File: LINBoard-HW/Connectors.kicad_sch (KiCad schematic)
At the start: 5 parts, among them J2 USB_C_Receptacle_USB2.0, J4 ATM13-6P-BM03

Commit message: board layout started
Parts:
- D14: footprint (none) -> Diode_SMD:D_SOD-123
- J4: value ATM13-6P-BM03 -> ATM15-6P-BM03; footprint (none) -> ATM:ATM13-6P
- R13, R14: footprint Resistor_SMD:R_0603_1608Metric -> Resistor_SMD:R_0402_1005Metric
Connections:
- net ENABLE is gone; now on net CAN_H: J4.4 (Pin_4)
- net CAN_H: no longer J4.2 (Pin_2)
- net GND: now also J4.5 (Pin_5)
- net LIN: now also J4.2 (Pin_2); no longer J4.5 (Pin_5)
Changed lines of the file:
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@@
+	)
+	(junction
+		(at 57.15 50.8)
+		(diameter 0)
+		(color 0 0 0 0)
 	)
 	(junction
@@
 	(wire
 		(pts
-			(xy 58.42 50.8) (xy 58.42 54.61)
+			(xy 57.15 48.26) (xy 57.15 50.8)
 		)
 		(stroke
@@
 	(wire
 		(pts
-			(xy 60.96 38.1) (xy 58.42 38.1)
+			(xy 53.34 38.1) (xy 60.96 38.1)
 		)
 		(stroke
@@
 	(wire
 		(pts
-			(xy 60.96 50.8) (xy 58.42 50.8)
-		)
-		(stroke
-			(width 0)
-			(type default)
-		)
-	)
-	(wire
-		(pts
 			(xy 54.61 113.03) (xy 63.5 113.03)
 		)
@@
 	(wire
 		(pts
+			(xy 57.15 50.8) (xy 60.96 50.8)
+		)
+		(stroke
+			(width 0)
+			(type default)
+		)
+	)
+	(wire
+		(pts
 			(xy 54.61 128.27) (xy 63.5 128.27)
 		)
@@
 	(wire
 		(pts
-			(xy 58.42 38.1) (xy 58.42 35.56)
+			(xy 57.15 50.8) (xy 57.15 58.42)
+		)
+		(stroke
+			(width 0)
+			(type default)
+		)
+	)
+	(wire
+		(pts
+			(xy 60.96 48.26) (xy 57.15 48.26)
+		)
+		(stroke
+			(width 0)
+			(type default)
+		)
+	)
+	(wire
+		(pts
+			(xy 53.34 38.1) (xy 53.34 35.56)
 		)
 		(stroke
@@
 	(hierarchical_label "CAN_H"
 		(shape bidirectional)
-		(at 60.96 40.64 180)
-		(effects
-			(font
-				(size 1.27 1.27)
-			)
-			(justify right)
-		)
-	)
-	(hierarchical_label "ENABLE"
-		(shape output)
 		(at 60.96 45.72 180)
 		(effects
@@
 	(hierarchical_label "LIN"
 		(shape bidirectional)
-		(at 60.96 48.26 180)
+		(at 60.96 40.64 180)
 		(effects
 			(font
@@
 			)
 		)
-		(property "Footprint" ""
+		(property "Footprint" "Diode_SMD:D_SOD-123"
 			(at 66.04 113.03 90)
 			(effects
@@
 	(symbol
 		(lib_id "power:+12V")
-		(at 58.42 35.56 0)
+		(at 53.34 35.56 0)
 		(unit 1)
 		(exclude_from_sim no)
@@
 		(on_board yes)
 		(dnp no)
-		(fields_autoplaced yes)
 		(property "Reference" "#PWR018"
-			(at 58.42 39.37 0)
+			(at 53.34 39.37 0)
 			(effects
 				(font
@@
 		)
 		(property "Value" "+12V"
-			(at 58.42 30.48 0)
+			(at 53.086 31.75 0)
 			(effects
 				(font
@@
 		)
 		(property "Footprint" ""
-			(at 58.42 35.56 0)
+			(at 53.34 35.56 0)
 			(effects
 				(font
@@
 		)
 		(property "Datasheet" ""
-			(at 58.42 35.56 0)
+			(at 53.34 35.56 0)
 			(effects
 				(font
@@
 		)
 		(property "Description" "Power symbol creates a global label with name \"+12V\""
-			(at 58.42 35.56 0)
+			(at 53.34 35.56 0)
 			(effects
 				(font
@@
 	(symbol
 		(lib_id "power:GND")
-		(at 58.42 54.61 0)
+		(at 57.15 58.42 0)
 		(unit 1)
 		(exclude_from_sim no)
@@
 		(fields_autoplaced yes)
 		(property "Reference" "#PWR019"
-			(at 58.42 60.96 0)
+			(at 57.15 64.77 0)
 			(effects
 				(font
@@
 		)
 		(property "Value" "GND"
-			(at 58.42 59.69 0)
+			(at 57.15 63.5 0)
 			(effects
 				(font
@@
 		)
 		(property "Footprint" ""
-			(at 58.42 54.61 0)
+			(at 57.15 58.42 0)
 			(effects
 				(font
@@
 		)
 		(property "Datasheet" ""
-			(at 58.42 54.61 0)
+			(at 57.15 58.42 0)
 			(effects
 				(font
@@
 		)
 		(property "Description" "Power symbol creates a global label with name \"GND\" , ground"
-			(at 58.42 54.61 0)
+			(at 57.15 58.42 0)
 			(effects
 				(font
@@
 			)
 		)
-		(property "Value" "ATM13-6P-BM03"
+		(property "Value" "ATM15-6P-BM03"
 			(at 68.58 45.7199 0)
 			(effects
@@
 			)
 		)
-		(property "Footprint" ""
+		(property "Footprint" "ATM:ATM13-6P"
 			(at 66.04 43.18 0)
 			(effects
@@
 			)
 		)
-		(property "Footprint" "Resistor_SMD:R_0603_1608Metric"
+		(property "Footprint" "Resistor_SMD:R_0402_1005Metric"
 			(at 80.01 123.19 0)
 			(effects
@@
 			)
 		)
-		(property "Footprint" "Resistor_SMD:R_0603_1608Metric"
+		(property "Footprint" "Resistor_SMD:R_0402_1005Metric"
 			(at 90.17 123.19 0)
 			(effects

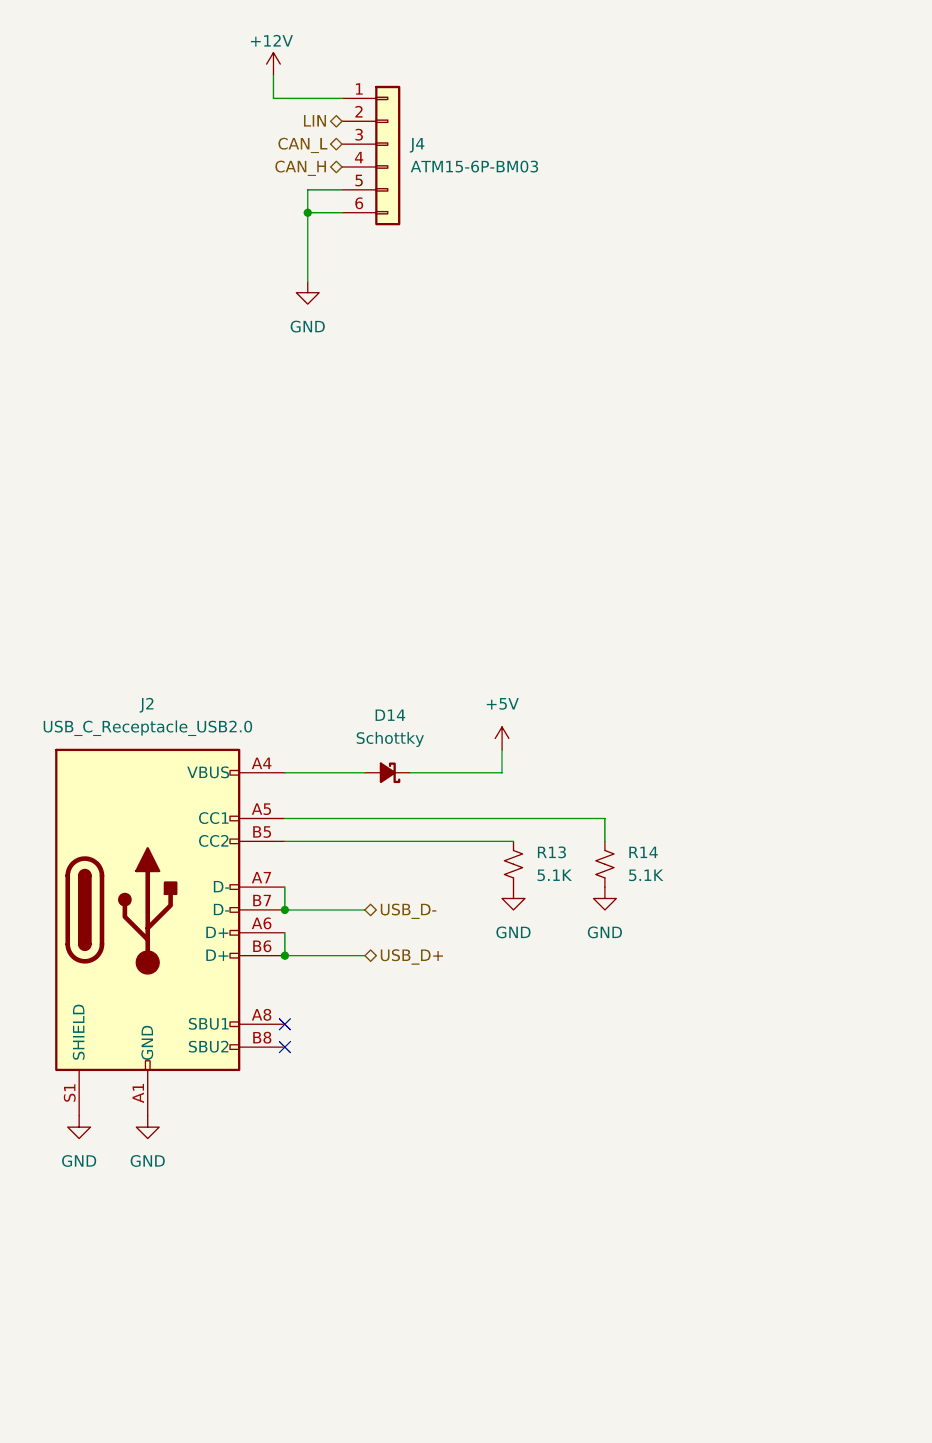
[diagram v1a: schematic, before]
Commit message: change usb
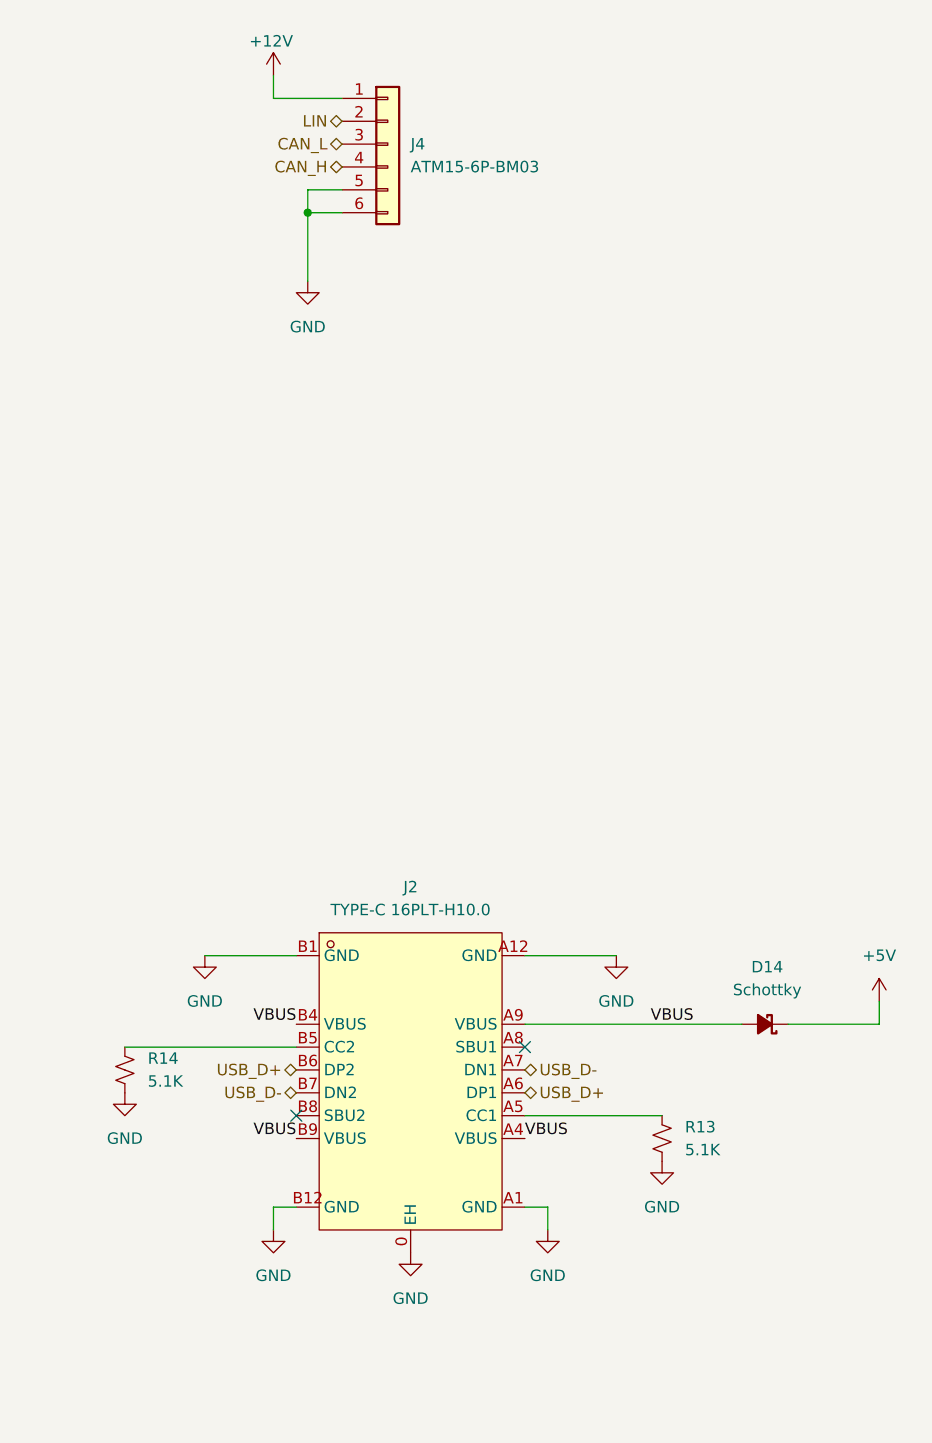
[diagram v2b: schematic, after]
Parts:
- removed J2: USB_C_Receptacle_USB2.0, Connector_USB:USB_C_Receptacle_GCT_USB4085, symbol Connectors:USB_C_Receptacle_USB2.0
- added J2: TYPE-C 16PLT-H10.0, vert_usb:TYPE-C-SMD_USB4120-03-C, symbol vert_usb:TYPE-C16PLT-H10.0
- J4: footprint ATM:ATM13-6P -> ATM:ATM15-6P_NoMountingHoles
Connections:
- net GND: now also J2.0 (EH), J2.A1 (GND), J2.A12 (GND), J2.B1 (GND), J2.B12 (GND)
- net USB_D+: now also J2.A6 (DP1), J2.B6 (DP2)
- net USB_D-: now also J2.A7 (DN1), J2.B7 (DN2)
- net VBUS: now reaches D14.2 (A)
- net VBUS: now also J2.A4 (VBUS), J2.A9 (VBUS), J2.B4 (VBUS), J2.B9 (VBUS)
- net at R14.1: now also J2.B5 (CC2)
- net at R13.1: now also J2.A5 (CC1)
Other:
- moved on the sheet: D14, R13, R14

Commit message: back to ra connectors
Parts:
- J2: footprint vert_usb:TYPE-C-SMD_USB4120-03-C -> Connector_USB:USB_C_Receptacle_GCT_USB4085
- J4: footprint ATM:ATM15-6P_NoMountingHoles -> ATM:ATM13-6P
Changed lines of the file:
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@@
 			)
 		)
-		(property "Footprint" "vert_usb:TYPE-C-SMD_USB4120-03-C"
+		(property "Footprint" "Connector_USB:USB_C_Receptacle_GCT_USB4085"
 			(at 68.58 173.99 0)
 			(effects
@@
 			)
 		)
-		(property "Footprint" "ATM:ATM15-6P_NoMountingHoles"
+		(property "Footprint" "ATM:ATM13-6P"
 			(at 66.04 43.18 0)
 			(effects

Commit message: doing some layout
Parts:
- R13, R14: footprint Resistor_SMD:R_0402_1005Metric -> Resistor_SMD:R_0805_2012Metric
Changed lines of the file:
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@@
 			)
 		)
-		(property "Footprint" "Resistor_SMD:R_0402_1005Metric"
+		(property "Footprint" "Resistor_SMD:R_0805_2012Metric"
 			(at 96.52 153.67 0)
 			(effects
@@
 			)
 		)
-		(property "Footprint" "Resistor_SMD:R_0402_1005Metric"
+		(property "Footprint" "Resistor_SMD:R_0805_2012Metric"
 			(at 36.83 146.05 0)
 			(effects

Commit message: routing first pass complete
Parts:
- removed J2: TYPE-C 16PLT-H10.0, Connector_USB:USB_C_Receptacle_GCT_USB4085, symbol vert_usb:TYPE-C16PLT-H10.0
- added J3: USB_C_Receptacle_USB2.0, Connector_USB:USB_C_Receptacle_GCT_USB4085, symbol Connectors:USB_C_Receptacle_USB2.0
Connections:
- net +12V: now also J4.6 (Pin_6); no longer J4.1 (Pin_1)
- net CAN_H: now also J4.2 (Pin_2); no longer J4.4 (Pin_4)
- net CAN_L: now also J4.1 (Pin_1); no longer J4.3 (Pin_3)
- net GND: now also J4.4 (Pin_4), J3.A1 (GND), J3.A12 (GND), J3.B1 (GND), J3.B12 (GND), J3.S1 (SHIELD); no longer J4.6 (Pin_6)
- net LIN: now also J4.3 (Pin_3); no longer J4.2 (Pin_2)
- net USB_D+: now also J3.A6 (D+), J3.B6 (D+)
- net USB_D-: now also J3.A7 (D-), J3.B7 (D-)
- net VBUS: now also J3.A4 (VBUS), J3.A9 (VBUS), J3.B4 (VBUS), J3.B9 (VBUS)
- net at R13.1: now also J3.A5 (CC1)
- net at R14.1: now also J3.B5 (CC2)
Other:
- moved on the sheet: D14, R13, R14

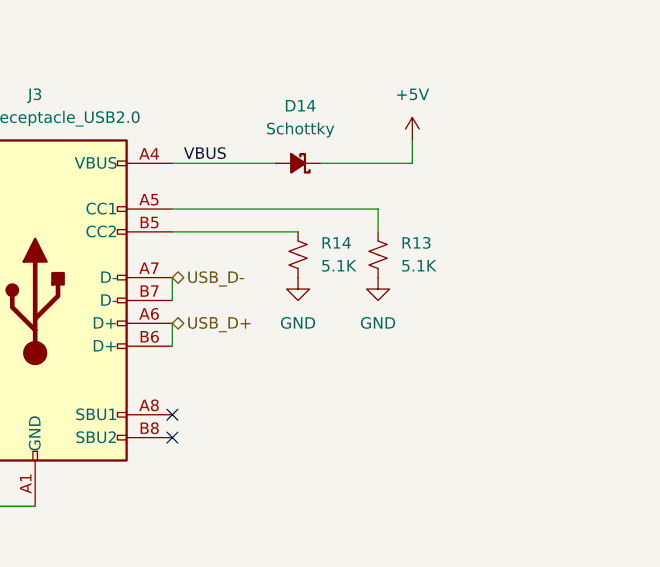
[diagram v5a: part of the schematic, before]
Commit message: fixed some trace widths
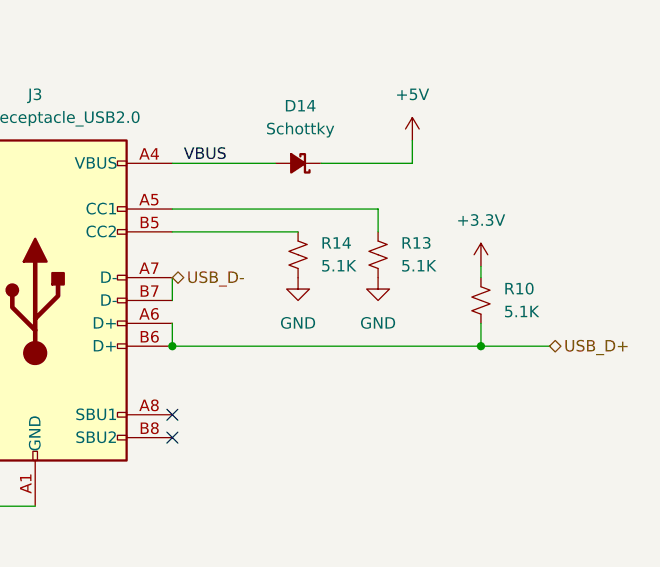
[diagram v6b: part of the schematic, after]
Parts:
- added R10: 5.1K, Resistor_SMD:R_0805_2012Metric, symbol Device:R_Small_US
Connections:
- net USB_D+: now also R10.2
- new net +3.3V: R10.1
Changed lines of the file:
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@@
+	)
+	(junction
+		(at 106.68 161.29)
+		(diameter 0)
+		(color 0 0 0 0)
 	)
 	(junction
@@
 		(color 0 0 0 0)
 	)
+	(junction
+		(at 72.39 161.29)
+		(diameter 0)
+		(color 0 0 0 0)
+	)
 	(no_connect
 		(at 72.39 168.91)
@@
 	(wire
 		(pts
+			(xy 106.68 158.75) (xy 106.68 161.29)
+		)
+		(stroke
+			(width 0)
+			(type default)
+		)
+	)
+	(wire
+		(pts
+			(xy 106.68 161.29) (xy 114.3 161.29)
+		)
+		(stroke
+			(width 0)
+			(type default)
+		)
+	)
+	(wire
+		(pts
+			(xy 106.68 152.4) (xy 106.68 153.67)
+		)
+		(stroke
+			(width 0)
+			(type default)
+		)
+	)
+	(wire
+		(pts
 			(xy 72.39 146.05) (xy 95.25 146.05)
 		)
@@
 		(pts
 			(xy 60.96 58.42) (xy 66.04 58.42)
+		)
+		(stroke
+			(width 0)
+			(type default)
+		)
+	)
+	(wire
+		(pts
+			(xy 72.39 161.29) (xy 106.68 161.29)
 		)
 		(stroke
@@
 	(hierarchical_label "USB_D+"
 		(shape bidirectional)
-		(at 72.39 158.75 0)
+		(at 114.3 161.29 0)
 		(effects
 			(font
@@
 	)
 	(symbol
+		(lib_id "power:+3.3V")
+		(at 106.68 152.4 0)
+		(unit 1)
+		(exclude_from_sim no)
+		(in_bom yes)
+		(on_board yes)
+		(dnp no)
+		(fields_autoplaced yes)
+		(property "Reference" "#PWR031"
+			(at 106.68 156.21 0)
+			(effects
+				(font
+					(size 1.27 1.27)
+				)
+				(hide yes)
+			)
+		)
+		(property "Value" "+3.3V"
+			(at 106.68 147.32 0)
+			(effects
+				(font
+					(size 1.27 1.27)
+				)
+			)
+		)
+		(property "Footprint" ""
+			(at 106.68 152.4 0)
+			(effects
+				(font
+					(size 1.27 1.27)
+				)
+				(hide yes)
+			)
+		)
+		(property "Datasheet" ""
+			(at 106.68 152.4 0)
+			(effects
+				(font
+					(size 1.27 1.27)
+				)
+				(hide yes)
+			)
+		)
+		(property "Description" "Power symbol creates a global label with name \"+3.3V\""
+			(at 106.68 152.4 0)
+			(effects
+				(font
+					(size 1.27 1.27)
+				)
+				(hide yes)
+			)
+		)
+		(pin "1"
+		)
+		(instances
+			(project "LINBoard-HW"
+				(path "/27863e5d-8a22-474c-850d-36d8970b0f4a/33375ab4-d724-4202-b76f-e99edd78e94c"
+					(reference "#PWR031")
+					(unit 1)
+				)
+			)
+		)
+	)
+	(symbol
 		(lib_id "power:GND")
 		(at 49.53 179.07 0)
@@
 					(unit 1)
 				)
+			)
+		)
+	)
+	(symbol
+		(lib_id "Device:R_Small_US")
+		(at 106.68 156.21 0)
+		(unit 1)
+		(exclude_from_sim no)
+		(in_bom yes)
+		(on_board yes)
+		(dnp no)
+		(fields_autoplaced yes)
+		(property "Reference" "R10"
+			(at 109.22 154.9399 0)
+			(effects
+				(font
+					(size 1.27 1.27)
+				)
+				(justify left)
+			)
+		)
+		(property "Value" "5.1K"
+			(at 109.22 157.4799 0)
+			(effects
+				(font
+					(size 1.27 1.27)
+				)
+				(justify left)
+			)
+		)
+		(property "Footprint" "Resistor_SMD:R_0805_2012Metric"
+			(at 106.68 156.21 0)
+			(effects
+				(font
+					(size 1.27 1.27)
+				)
+				(hide yes)
+			)
+		)
+		(property "Datasheet" "~"
+			(at 106.68 156.21 0)
+			(effects
+				(font
+					(size 1.27 1.27)
+				)
+				(hide yes)
+			)
+		)
+		(property "Description" "Resistor, small US symbol"
+			(at 106.68 156.21 0)
+			(effects
+				(font
+					(size 1.27 1.27)
+				)
+				(hide yes)
+			)
+		)
+		(pin "2"
+		)
+		(pin "1"
+		)
+		(instances
+			(project "LINBoard-HW"
+				(path "/27863e5d-8a22-474c-850d-36d8970b0f4a/33375ab4-d724-4202-b76f-e99edd78e94c"
+					(reference "R10")
+					(unit 1)
+				)

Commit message: add fab outputs
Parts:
- D14: LCSC Part (none) -> C179426
- J3, J4: now left out of the parts list
- R10, R13, R14: LCSC Part (none) -> C218638
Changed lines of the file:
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@@
+			)
+		)
+		(property "LCSC Part" "C179426"
+			(at 86.36 140.97 0)
+			(effects
+				(font
+					(size 1.27 1.27)
+				)
+				(hide yes)
 			)
 		)
@@
 		(unit 1)
 		(exclude_from_sim no)
-		(in_bom yes)
+		(in_bom no)
 		(on_board yes)
 		(dnp no)
@@
 			)
 		)
+		(property "LCSC Part" ""
+			(at 66.04 43.18 0)
+			(effects
+				(font
+					(size 1.27 1.27)
+				)
+				(hide yes)
+			)
+		)
 		(pin "1"
 		)
@@
 			)
 		)
+		(property "LCSC Part" "C218638"
+			(at 95.25 151.13 0)
+			(effects
+				(font
+					(size 1.27 1.27)
+				)
+				(hide yes)
+			)
+		)
 		(pin "2"
 		)
@@
 			)
 		)
+		(property "LCSC Part" "C218638"
+			(at 106.68 156.21 0)
+			(effects
+				(font
+					(size 1.27 1.27)
+				)
+				(hide yes)
+			)
+		)
 		(pin "2"
 		)
@@
 			)
 		)
+		(property "LCSC Part" "C218638"
+			(at 86.36 151.13 0)
+			(effects
+				(font
+					(size 1.27 1.27)
+				)
+				(hide yes)
+			)
+		)
 		(pin "2"
 		)
@@
 		(unit 1)
 		(exclude_from_sim no)
-		(in_bom yes)
+		(in_bom no)
 		(on_board yes)
 		(dnp no)
@@
 			(at 57.15 156.21 0)
 			(effects
+				(font
+					(size 1.27 1.27)
+				)
+				(hide yes)
+			)
+		)
+		(property "LCSC Part" ""
+			(at 57.15 156.21 0)
+			(effects

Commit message: change pinout, export
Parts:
- R10, R13, R14: LCSC Part C218638 -> C27834
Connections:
- net GND: no longer J4.4 (Pin_4)
- net LIN: now also J4.4 (Pin_4)
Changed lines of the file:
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@@
+	)
+	(junction
+		(at 59.69 43.18)
+		(diameter 0)
+		(color 0 0 0 0)
 	)
 	(junction
@@
 	)
 	(junction
-		(at 57.15 48.26)
-		(diameter 0)
-		(color 0 0 0 0)
-	)
-	(junction
 		(at 72.39 161.29)
 		(diameter 0)
@@
 	(wire
 		(pts
-			(xy 57.15 45.72) (xy 57.15 48.26)
-		)
-		(stroke
-			(width 0)
-			(type default)
-		)
-	)
-	(wire
-		(pts
 			(xy 72.39 153.67) (xy 72.39 156.21)
 		)
@@
 	(wire
 		(pts
+			(xy 59.69 43.18) (xy 60.96 43.18)
+		)
+		(stroke
+			(width 0)
+			(type default)
+		)
+	)
+	(wire
+		(pts
+			(xy 58.42 43.18) (xy 59.69 43.18)
+		)
+		(stroke
+			(width 0)
+			(type default)
+		)
+	)
+	(wire
+		(pts
 			(xy 88.9 140.97) (xy 99.06 140.97)
 		)
@@
 	(wire
 		(pts
+			(xy 60.96 45.72) (xy 59.69 45.72)
+		)
+		(stroke
+			(width 0)
+			(type default)
+		)
+	)
+	(wire
+		(pts
 			(xy 57.15 48.26) (xy 57.15 55.88)
 		)
@@
 	(wire
 		(pts
+			(xy 59.69 43.18) (xy 59.69 45.72)
+		)
+		(stroke
+			(width 0)
+			(type default)
+		)
+	)
+	(wire
+		(pts
 			(xy 72.39 158.75) (xy 72.39 161.29)
-		)
-		(stroke
-			(width 0)
-			(type default)
-		)
-	)
-	(wire
-		(pts
-			(xy 60.96 45.72) (xy 57.15 45.72)
 		)
 		(stroke
@@
 	(hierarchical_label "LIN"
 		(shape bidirectional)
-		(at 60.96 43.18 180)
+		(at 58.42 43.18 180)
 		(effects
 			(font
@@
 			)
 		)
-		(property "LCSC Part" "C218638"
+		(property "LCSC Part" "C27834"
 			(at 95.25 151.13 0)
 			(effects
@@
 			)
 		)
-		(property "LCSC Part" "C218638"
+		(property "LCSC Part" "C27834"
 			(at 106.68 156.21 0)
 			(effects
@@
 			)
 		)
-		(property "LCSC Part" "C218638"
+		(property "LCSC Part" "C27834"
 			(at 86.36 151.13 0)
 			(effects
